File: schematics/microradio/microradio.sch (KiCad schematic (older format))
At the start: 3 parts, among them U1 NodeMCU1.0(ESP-12E), U2 23LC1024, U3 PCM5102A

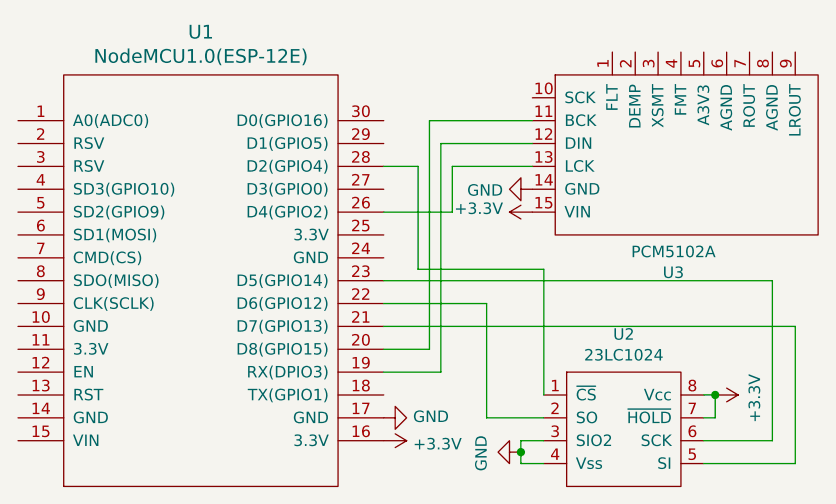
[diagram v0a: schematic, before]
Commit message: Fix pcm5102 vcc
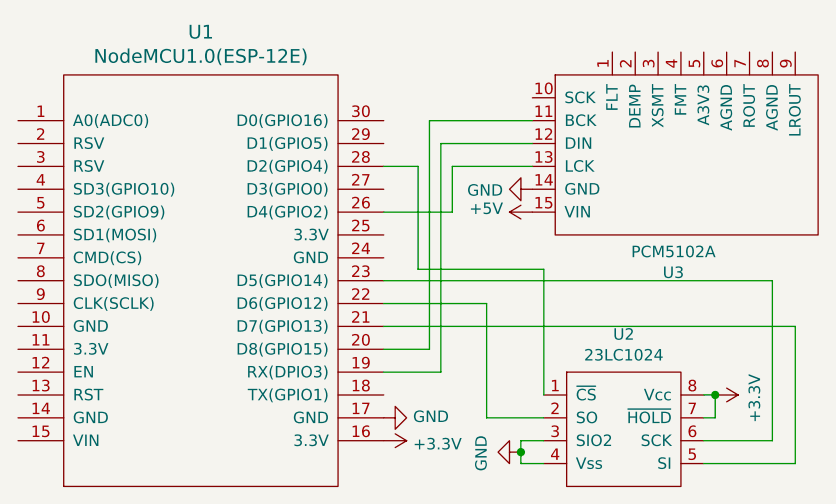
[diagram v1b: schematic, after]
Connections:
- net +3V3: no longer U3.15 (VIN)
- new net +5V: U3.15 (VIN)
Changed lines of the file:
@@
 	5900 2750 5900 2950
-$Comp
-L power:+3.3V #PWR0103
-U 1 1 5F4A5BEB
-P 6250 2950
-F 0 "#PWR0103" H 6250 2800 50  0001 C CNN
-F 1 "+3.3V" V 6265 3078 50  0000 L CNN
-F 2 "" H 6250 2950 50  0001 C CNN
-F 3 "" H 6250 2950 50  0001 C CNN
-	1    6250 2950
-	0    -1   -1   0
-$EndComp
 $Comp
 L power:GND #PWR0104
@@
 Wire Wire Line
 	5600 3250 7300 3250
+$Comp
+L power:+5V #PWR?
+U 1 1 5F5BABCB
+P 6250 2950
+F 0 "#PWR?" H 6250 2800 50  0001 C CNN
+F 1 "+5V" V 6265 3078 50  0000 L CNN
+F 2 "" H 6250 2950 50  0001 C CNN
+F 3 "" H 6250 2950 50  0001 C CNN
+	1    6250 2950
+	0    -1   -1   0
+$EndComp
 $EndSCHEMATC
